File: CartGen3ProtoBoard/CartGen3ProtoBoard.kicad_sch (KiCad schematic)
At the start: 0 parts

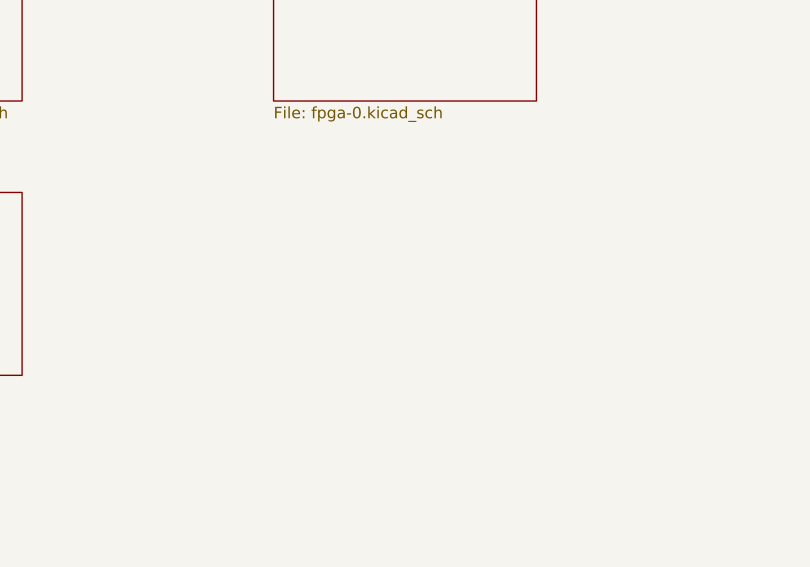
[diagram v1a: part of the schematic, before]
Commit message: Added audio schematic
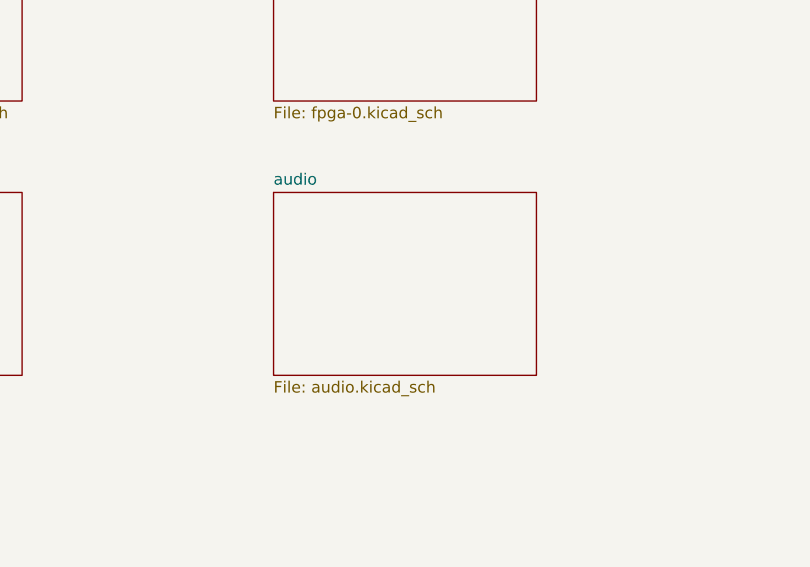
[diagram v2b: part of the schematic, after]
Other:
- added sheet audio (audio.kicad_sch)
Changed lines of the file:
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@@
+    )
+  )
+  (sheet (at 127 102.87) (size 29.21 20.32) (fields_autoplaced)
+    (stroke (width 0.1524) (type solid) (color 0 0 0 0))
+    (fill (color 0 0 0 0.0000))
+    (property "Sheet name" "audio" (id 0) (at 127 102.1584 0)
+      (effects (font (size 1.27 1.27)) (justify left bottom))
+    )
+    (property "Sheet file" "audio.kicad_sch" (id 1) (at 127 123.7746 0)
+      (effects (font (size 1.27 1.27)) (justify left top))
     )
   )
@@
     (path "/af356851-5ece-4832-ae35-3dccdb32b1b1" (page "5"))
     (path "/4b2118cf-fb52-4113-a818-0a42fecbb1e6" (page "6"))
+    (path "/73c1eee2-05c6-471c-a3e5-93be837b155c" (page "7"))
   )
   (symbol_instances
@@
       (reference "#PWR011") (unit 1) (value "GND") (footprint "")
     )
+    (path "/73c1eee2-05c6-471c-a3e5-93be837b155c/ce69169d-a0c9-4535-81e6-d49c354f4739"
+      (reference "#PWR012") (unit 1) (value "+5V") (footprint "")
+    )
+    (path "/73c1eee2-05c6-471c-a3e5-93be837b155c/ba08af7e-b791-4509-9e28-3aa7e630b573"
+      (reference "#PWR013") (unit 1) (value "GND") (footprint "")
+    )
+    (path "/73c1eee2-05c6-471c-a3e5-93be837b155c/9d642235-ec73-4c0b-bcb4-693f9c6ab26b"
+      (reference "#PWR014") (unit 1) (value "GND") (footprint "")
+    )
+    (path "/73c1eee2-05c6-471c-a3e5-93be837b155c/1a8d6324-fabc-4580-9cf4-5d0f64c57614"
+      (reference "#PWR015") (unit 1) (value "GND") (footprint "")
+    )
+    (path "/73c1eee2-05c6-471c-a3e5-93be837b155c/fa726952-0ffe-462f-a32b-4cf1be423fcf"
+      (reference "#PWR016") (unit 1) (value "GND") (footprint "")
+    )
+    (path "/73c1eee2-05c6-471c-a3e5-93be837b155c/d353044a-8636-4ba3-a449-e69def513409"
+      (reference "#PWR017") (unit 1) (value "GND") (footprint "")
+    )
+    (path "/73c1eee2-05c6-471c-a3e5-93be837b155c/e3cd2cce-8f4a-4cfe-9429-3267b17a5ff8"
+      (reference "#PWR018") (unit 1) (value "GND") (footprint "")
+    )
+    (path "/73c1eee2-05c6-471c-a3e5-93be837b155c/17b787ff-0994-4a57-8ec9-aa2256743d06"
+      (reference "#PWR019") (unit 1) (value "GND") (footprint "")
+    )
     (path "/f06d5139-8321-4854-8742-7179642a0021/039539dc-9afa-48a1-bd79-180ff497c6cb"
       (reference "#PWR0101") (unit 1) (value "+3V3") (footprint "")
@@
       (reference "#PWR0121") (unit 1) (value "+3.3V") (footprint "")
     )
+    (path "/c435552a-e81e-4e91-8943-4d198d361cb8/8cf90fa2-9923-4191-955c-16eee1d5441d"
+      (reference "#PWR?") (unit 1) (value "+5V") (footprint "")
+    )
     (path "/c435552a-e81e-4e91-8943-4d198d361cb8/69b6419d-0162-44a2-b441-9c8586353b81"
       (reference "A1") (unit 1) (value "GBC_Cart") (footprint "Boards:GBC_Cart")
@@
       (reference "C15") (unit 1) (value "0.01uF") (footprint "")
     )
+    (path "/73c1eee2-05c6-471c-a3e5-93be837b155c/d40b93f4-e5ce-4496-b305-582815640b32"
+      (reference "C16") (unit 1) (value "100N") (footprint "")
+    )
+    (path "/73c1eee2-05c6-471c-a3e5-93be837b155c/51df258e-dfe3-4c62-9101-c990ba6a19a6"
+      (reference "C17") (unit 1) (value "820P") (footprint "")
+    )
+    (path "/73c1eee2-05c6-471c-a3e5-93be837b155c/ad288c61-5b0c-40db-a8c3-2211b0dd5a3a"
+      (reference "C18") (unit 1) (value "82P") (footprint "")
+    )
+    (path "/73c1eee2-05c6-471c-a3e5-93be837b155c/75a9ffd0-6d9e-4d55-bd93-1b1ce7e243dc"
+      (reference "C19") (unit 1) (value "820P") (footprint "")
+    )
+    (path "/73c1eee2-05c6-471c-a3e5-93be837b155c/fff92b55-e8f9-44c9-bcc2-76cc02092ca8"
+      (reference "C20") (unit 1) (value "470P") (footprint "")
+    )
+    (path "/73c1eee2-05c6-471c-a3e5-93be837b155c/504d6a0a-ed6c-440f-ae9d-d48f75267748"
+      (reference "C21") (unit 1) (value "100N") (footprint "")
+    )
     (path "/c435552a-e81e-4e91-8943-4d198d361cb8/1a03c680-6df4-4ad6-b0ee-2551be034eac"
       (reference "J1") (unit 1) (value "Conn_01x02_Male") (footprint "")
@@
       (reference "R1") (unit 1) (value "15K") (footprint "")
     )
+    (path "/73c1eee2-05c6-471c-a3e5-93be837b155c/d9da992c-40d4-4ad0-a2f7-90881b460125"
+      (reference "R8") (unit 1) (value "6K8") (footprint "")
+    )
+    (path "/73c1eee2-05c6-471c-a3e5-93be837b155c/f411b778-3c7a-434c-b87b-ffb4ee5ec880"
+      (reference "R9") (unit 1) (value "120K") (footprint "")
+    )
+    (path "/73c1eee2-05c6-471c-a3e5-93be837b155c/957d3c53-d771-46db-870d-6c905335654b"
+      (reference "R10") (unit 1) (value "1K") (footprint "")
+    )
+    (path "/73c1eee2-05c6-471c-a3e5-93be837b155c/839682a1-1960-40a2-85cd-a5969e23e021"
+      (reference "R11") (unit 1) (value "10K") (footprint "")
+    )
+    (path "/73c1eee2-05c6-471c-a3e5-93be837b155c/058a981e-46ea-4230-b063-42f6c31bbd7d"
+      (reference "R12") (unit 1) (value "39K") (footprint "")
+    )
+    (path "/73c1eee2-05c6-471c-a3e5-93be837b155c/f7435aa5-2dd1-4d0e-9160-9e8a6233a92a"
+      (reference "R13") (unit 1) (value "10K") (footprint "")
+    )
+    (path "/73c1eee2-05c6-471c-a3e5-93be837b155c/80556cb5-d678-49ef-8500-e5ea1deabb84"
+      (reference "R14") (unit 1) (value "220K") (footprint "")
+    )
     (path "/f06d5139-8321-4854-8742-7179642a0021/f9ff6040-eb0b-4741-92e7-afad23017813"
       (reference "SW1") (unit 1) (value "SW_Push_Dual") (footprint "")
@@
       (reference "U4") (unit 1) (value "AS4C32M8SA") (footprint "")
     )
-  )
+    (path "/73c1eee2-05c6-471c-a3e5-93be837b155c/53b15f8d-2bd4-4e8b-a7f8-9bcd21dfe18c"
+      (reference "U8") (unit 1) (value "LM358") (footprint "")
+    )
+    (path "/73c1eee2-05c6-471c-a3e5-93be837b155c/988b05c2-3359-4aac-b98b-94b8b7adc93a"
+      (reference "U8") (unit 2) (value "LM358") (footprint "")
+    )
+    (path "/73c1eee2-05c6-471c-a3e5-93be837b155c/8a329812-d971-4a7f-8df2-892e21b2571c"
+      (reference "U8") (unit 3) (value "LM358") (footprint "")
+    )
+  )

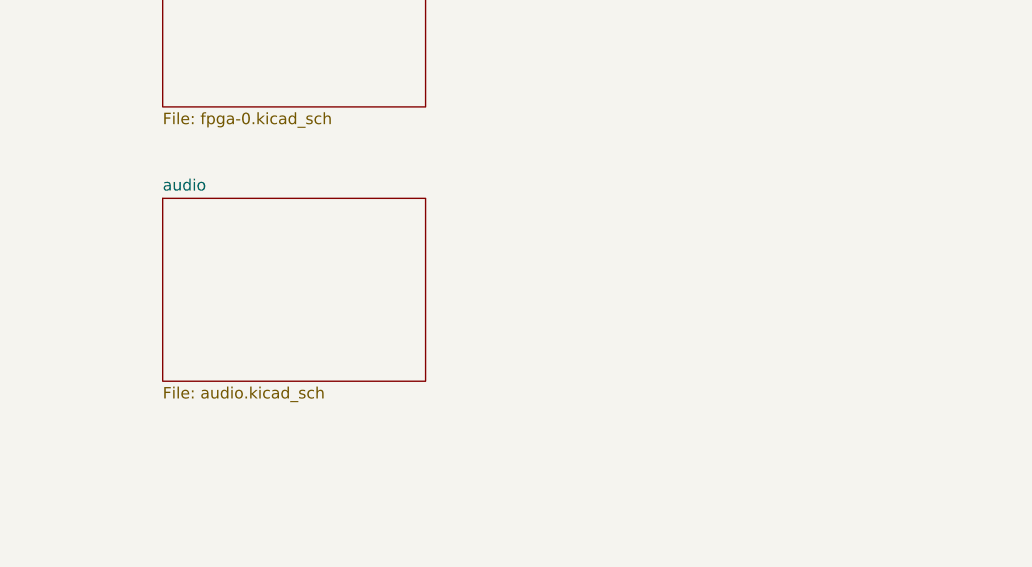
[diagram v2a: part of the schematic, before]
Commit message: Added audio_mixer schematic
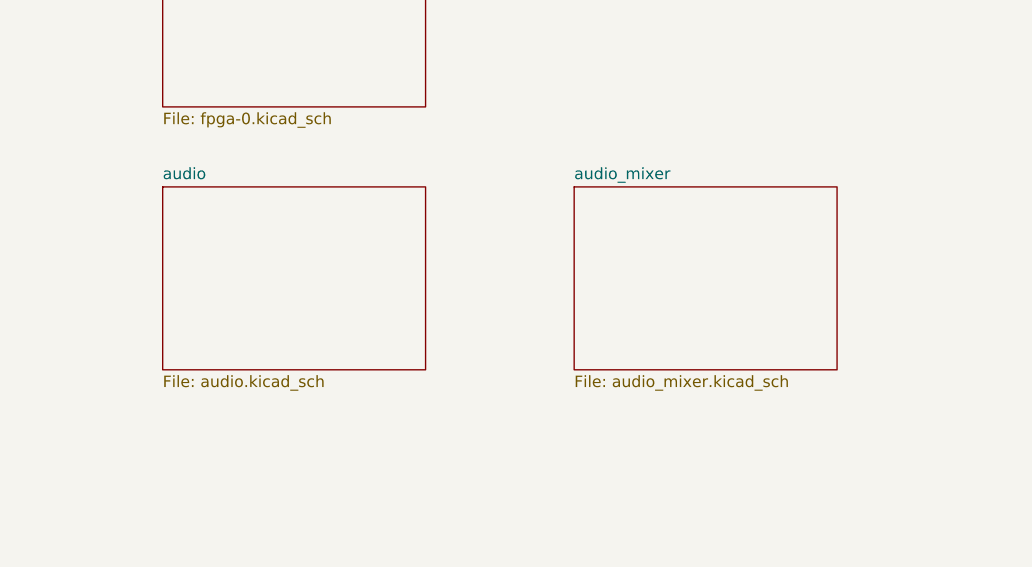
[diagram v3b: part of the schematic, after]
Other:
- added sheet audio_mixer (audio_mixer.kicad_sch)
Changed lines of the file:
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@@
     )
   )
-  (sheet (at 127 102.87) (size 29.21 20.32) (fields_autoplaced)
+  (sheet (at 127 101.6) (size 29.21 20.32) (fields_autoplaced)
     (stroke (width 0.1524) (type solid) (color 0 0 0 0))
     (fill (color 0 0 0 0.0000))
-    (property "Sheet name" "audio" (id 0) (at 127 102.1584 0)
+    (property "Sheet name" "audio" (id 0) (at 127 100.8884 0)
       (effects (font (size 1.27 1.27)) (justify left bottom))
     )
-    (property "Sheet file" "audio.kicad_sch" (id 1) (at 127 123.7746 0)
+    (property "Sheet file" "audio.kicad_sch" (id 1) (at 127 122.5046 0)
       (effects (font (size 1.27 1.27)) (justify left top))
     )
@@
     )
     (property "Sheet file" "power-and-connectors.kicad_sch" (id 1) (at 27.94 93.2946 0)
+      (effects (font (size 1.27 1.27)) (justify left top))
+    )
+  )
+  (sheet (at 172.72 101.6) (size 29.21 20.32) (fields_autoplaced)
+    (stroke (width 0.1524) (type solid) (color 0 0 0 0))
+    (fill (color 0 0 0 0.0000))
+    (property "Sheet name" "audio_mixer" (id 0) (at 172.72 100.8884 0)
+      (effects (font (size 1.27 1.27)) (justify left bottom))
+    )
+    (property "Sheet file" "audio_mixer.kicad_sch" (id 1) (at 172.72 122.5046 0)
       (effects (font (size 1.27 1.27)) (justify left top))
     )
@@
     (path "/4b2118cf-fb52-4113-a818-0a42fecbb1e6" (page "6"))
     (path "/73c1eee2-05c6-471c-a3e5-93be837b155c" (page "7"))
+    (path "/ebeeec6e-78d4-4657-a845-c0d00b5092fb" (page "8"))
   )
   (symbol_instances
@@
       (reference "#PWR019") (unit 1) (value "GND") (footprint "")
     )
+    (path "/ebeeec6e-78d4-4657-a845-c0d00b5092fb/f4158918-fc39-47aa-8f96-487334c37eb7"
+      (reference "#PWR020") (unit 1) (value "GND") (footprint "")
+    )
+    (path "/ebeeec6e-78d4-4657-a845-c0d00b5092fb/5e95db06-7439-4544-b6f8-d899b9e94e75"
+      (reference "#PWR021") (unit 1) (value "GND") (footprint "")
+    )
+    (path "/ebeeec6e-78d4-4657-a845-c0d00b5092fb/e27ba004-88e0-4271-aaf5-62a519e7ff37"
+      (reference "#PWR022") (unit 1) (value "GND") (footprint "")
+    )
+    (path "/ebeeec6e-78d4-4657-a845-c0d00b5092fb/2288e2dd-85b3-4081-8f1e-6bd47ea0e1b7"
+      (reference "#PWR023") (unit 1) (value "GND") (footprint "")
+    )
+    (path "/ebeeec6e-78d4-4657-a845-c0d00b5092fb/4422e03a-d978-488b-a5de-43e41167c443"
+      (reference "#PWR024") (unit 1) (value "GND") (footprint "")
+    )
+    (path "/ebeeec6e-78d4-4657-a845-c0d00b5092fb/65fa977a-133b-4cf3-b804-3616c72e97c0"
+      (reference "#PWR025") (unit 1) (value "GND") (footprint "")
+    )
+    (path "/ebeeec6e-78d4-4657-a845-c0d00b5092fb/6359a56a-90be-4fbc-a574-1dfce54d1d09"
+      (reference "#PWR026") (unit 1) (value "GND") (footprint "")
+    )
+    (path "/ebeeec6e-78d4-4657-a845-c0d00b5092fb/9a175871-e0fe-4ac6-8d11-05000d96e38d"
+      (reference "#PWR027") (unit 1) (value "+5V") (footprint "")
+    )
+    (path "/ebeeec6e-78d4-4657-a845-c0d00b5092fb/3389ab43-fe6a-4271-b43d-0322e08296db"
+      (reference "#PWR028") (unit 1) (value "GND") (footprint "")
+    )
+    (path "/ebeeec6e-78d4-4657-a845-c0d00b5092fb/7156eb4c-458f-4fad-b24f-29ceaf0dff91"
+      (reference "#PWR029") (unit 1) (value "GND") (footprint "")
+    )
+    (path "/ebeeec6e-78d4-4657-a845-c0d00b5092fb/8c709c70-4f75-4147-aaea-59013ec10892"
+      (reference "#PWR030") (unit 1) (value "GND") (footprint "")
+    )
     (path "/f06d5139-8321-4854-8742-7179642a0021/039539dc-9afa-48a1-bd79-180ff497c6cb"
       (reference "#PWR0101") (unit 1) (value "+3V3") (footprint "")
@@
       (reference "C21") (unit 1) (value "100N") (footprint "")
     )
+    (path "/ebeeec6e-78d4-4657-a845-c0d00b5092fb/a988d232-8531-49ea-aae3-66b8dc43b861"
+      (reference "C22") (unit 1) (value "820P") (footprint "")
+    )
+    (path "/ebeeec6e-78d4-4657-a845-c0d00b5092fb/5c3e5f78-ef90-4d70-8cdd-4b04cdf56a3f"
+      (reference "C23") (unit 1) (value "820P") (footprint "")
+    )
+    (path "/ebeeec6e-78d4-4657-a845-c0d00b5092fb/669a63b7-a468-41ae-99e9-ddffd0e2e578"
+      (reference "C24") (unit 1) (value "820P") (footprint "")
+    )
+    (path "/ebeeec6e-78d4-4657-a845-c0d00b5092fb/a37ca12b-5233-43ad-bbc5-eb0f992f7532"
+      (reference "C25") (unit 1) (value "820P") (footprint "")
+    )
+    (path "/ebeeec6e-78d4-4657-a845-c0d00b5092fb/aeeff82a-cd72-4c1f-a4ba-9dd821b77c12"
+      (reference "C26") (unit 1) (value "820P") (footprint "")
+    )
+    (path "/ebeeec6e-78d4-4657-a845-c0d00b5092fb/cef49d78-a8d9-4fab-b636-c0845962862e"
+      (reference "C27") (unit 1) (value "82P") (footprint "")
+    )
+    (path "/ebeeec6e-78d4-4657-a845-c0d00b5092fb/4cd1da7e-dd77-427d-86ce-e922bf4fe7a0"
+      (reference "C28") (unit 1) (value "100N") (footprint "")
+    )
+    (path "/ebeeec6e-78d4-4657-a845-c0d00b5092fb/8af70cd2-72a1-47fa-940c-8aec358d7238"
+      (reference "C29") (unit 1) (value "470P") (footprint "")
+    )
+    (path "/ebeeec6e-78d4-4657-a845-c0d00b5092fb/3e36572e-6a7d-4226-804e-c8a0e1703898"
+      (reference "C30") (unit 1) (value "100N") (footprint "")
+    )
     (path "/c435552a-e81e-4e91-8943-4d198d361cb8/1a03c680-6df4-4ad6-b0ee-2551be034eac"
       (reference "J1") (unit 1) (value "Conn_01x02_Male") (footprint "")
@@
       (reference "R14") (unit 1) (value "220K") (footprint "")
     )
+    (path "/ebeeec6e-78d4-4657-a845-c0d00b5092fb/a2d23dd2-0be0-4cfc-b271-ababa43b2f59"
+      (reference "R15") (unit 1) (value "10K") (footprint "")
+    )
+    (path "/ebeeec6e-78d4-4657-a845-c0d00b5092fb/1a393db0-82b5-4784-97f4-ceb41cc1ce00"
+      (reference "R16") (unit 1) (value "10K") (footprint "")
+    )
+    (path "/ebeeec6e-78d4-4657-a845-c0d00b5092fb/dcef4ff3-3702-4cc6-94a1-cd749a128d7b"
+      (reference "R17") (unit 1) (value "10K") (footprint "")
+    )
+    (path "/ebeeec6e-78d4-4657-a845-c0d00b5092fb/75ae2783-3198-4f8d-9057-5e2819e15a3b"
+      (reference "R18") (unit 1) (value "10K") (footprint "")
+    )
+    (path "/ebeeec6e-78d4-4657-a845-c0d00b5092fb/da19c195-6c6c-49e8-939b-1c592390049a"
+      (reference "R19") (unit 1) (value "100K") (footprint "")
+    )
+    (path "/ebeeec6e-78d4-4657-a845-c0d00b5092fb/bd156ba5-7fdc-425a-bb4e-12cab9a343f1"
+      (reference "R20") (unit 1) (value "100K") (footprint "")
+    )
+    (path "/ebeeec6e-78d4-4657-a845-c0d00b5092fb/ec58d493-fe15-43a8-a97a-862eec29d1c5"
+      (reference "R21") (unit 1) (value "100K") (footprint "")
+    )
+    (path "/ebeeec6e-78d4-4657-a845-c0d00b5092fb/3734387d-344c-4dc3-9692-04b3d047a449"
+      (reference "R22") (unit 1) (value "100K") (footprint "")
+    )
+    (path "/ebeeec6e-78d4-4657-a845-c0d00b5092fb/5bbf070e-2efd-4e21-b379-d12649dfed08"
+      (reference "R23") (unit 1) (value "1M") (footprint "")
+    )
+    (path "/ebeeec6e-78d4-4657-a845-c0d00b5092fb/2bad68aa-9e7f-43c9-a7b1-54fefed038ad"
+      (reference "R24") (unit 1) (value "6K8") (footprint "")
+    )
+    (path "/ebeeec6e-78d4-4657-a845-c0d00b5092fb/c2ce2c33-37be-4612-bb20-90ac598b1de8"
+      (reference "R25") (unit 1) (value "120K") (footprint "")
+    )
+    (path "/ebeeec6e-78d4-4657-a845-c0d00b5092fb/6722264c-0208-4da9-9f86-0b87b5f5f70d"
+      (reference "R26") (unit 1) (value "39K") (footprint "")
+    )
+    (path "/ebeeec6e-78d4-4657-a845-c0d00b5092fb/bf8789fb-bf0e-43cf-aec6-8b66e3f21676"
+      (reference "R27") (unit 1) (value "10K") (footprint "")
+    )
+    (path "/ebeeec6e-78d4-4657-a845-c0d00b5092fb/baae0a6d-4348-48f8-8641-83ee2ae7acd7"
+      (reference "R28") (unit 1) (value "220K") (footprint "")
+    )
     (path "/f06d5139-8321-4854-8742-7179642a0021/f9ff6040-eb0b-4741-92e7-afad23017813"
       (reference "SW1") (unit 1) (value "SW_Push_Dual") (footprint "")
@@
       (reference "U8") (unit 3) (value "LM358") (footprint "")
     )
-  )
+    (path "/ebeeec6e-78d4-4657-a845-c0d00b5092fb/d21943bd-035d-4d62-bee1-14243387acb7"
+      (reference "U9") (unit 1) (value "LM358") (footprint "")
+    )
+    (path "/ebeeec6e-78d4-4657-a845-c0d00b5092fb/f0b25512-22b5-4a91-87af-b5c076c89f21"
+      (reference "U9") (unit 2) (value "LM358") (footprint "")
+    )
+    (path "/ebeeec6e-78d4-4657-a845-c0d00b5092fb/e538e739-1aea-47e6-a776-6d5c887d1e5e"
+      (reference "U9") (unit 3) (value "LM358") (footprint "")
+    )
+  )
